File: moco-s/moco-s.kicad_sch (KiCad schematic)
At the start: 34 parts, among them J1 Conn_01x06, J2 Conn_01x02, J3 Conn_01x09, J5 Debug, SW1 SW_Push, SW2 SW_Push, U1 XC6220B331MR

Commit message: Update ref
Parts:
- renumbered C2 to C1, C6 to C2, C8 to C3, H3 to H1, H1 to H2, H4 to H3, H2 to H4, J5 to J2, J2 to J3, J3 to J4, R6 to R1, R14 to R10, R17 to R11, R18 to R12, R8 to R2, R11 to R3, R15 to R4, R16 to R5, R13 to R6, R1 to R7, R2 to R8, R3 to R9, SB7 to SB1, JP1 to SB2, JP2 to SB3, JP3 to SB4, SB4 to SB5, TP3 to TP1, TP5 to TP2

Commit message: Use kelvin connection for shunt resistance
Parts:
- C3: JLCPCB Part # (none) -> C368809; MFR.Part # (none) -> CL05A475KP5NRNC
- J1: JLCPCB Part # (none) -> C2829255; MFR.Part # (none) -> GH1.25-6PWBPZ
- J3: JLCPCB Part # (none) -> C98733; MFR.Part # (none) -> XT60
- J4: JLCPCB Part # (none) -> C2829258; MFR.Part # (none) -> GH1.25-9PWBPZ
- R7: JLCPCB Part # (none) -> C25172; MFR.Part # (none) -> 0402WGJ0561TCE
- R8, R9: JLCPCB Part # (none) -> C105876; MFR.Part # (none) -> RC0402JR-07330RL
- SB2, SB3, SB4: now left out of the parts list
- SW1, SW2: JLCPCB Part # (none) -> C520860; MFR.Part # (none) -> TS-1092S-B3D2-G
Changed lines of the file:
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@@
   (title_block
     (title "MoCo-S")
+    (rev "1.0")
   )
   (junction (at 77.47 137.16) (diameter 0) (color 0 0 0 0)
@@
   )
   (symbol (lib_id "Jumper:SolderJumper_3_Open") (at 200.66 64.77 90) (unit 1)
-    (in_bom yes) (on_board yes)
+    (in_bom no) (on_board yes)
     (property "Reference" "SB2" (id 0) (at 198.12 64.77 90)
       (effects (font (size 1.27 1.27)) (justify left))
@@
     )
     (property "Datasheet" "~" (id 3) (at 72.39 142.24 0)
+      (effects (font (size 1.27 1.27)) hide)
+    )
+    (property "JLCPCB Part #" "C520860" (id 4) (at 77.47 142.24 0)
+      (effects (font (size 1.27 1.27)) hide)
+    )
+    (property "MFR.Part #" "TS-1092S-B3D2-G" (id 5) (at 77.47 142.24 0)
       (effects (font (size 1.27 1.27)) hide)
     )
@@
     )
     (property "Datasheet" "~" (id 3) (at 41.91 133.35 0)
+      (effects (font (size 1.27 1.27)) hide)
+    )
+    (property "JLCPCB Part #" "C520860" (id 4) (at 46.99 133.35 0)
+      (effects (font (size 1.27 1.27)) hide)
+    )
+    (property "MFR.Part #" "TS-1092S-B3D2-G" (id 5) (at 46.99 133.35 0)
       (effects (font (size 1.27 1.27)) hide)
     )
@@
   )
   (symbol (lib_id "Jumper:SolderJumper_3_Open") (at 200.66 81.28 90) (unit 1)
-    (in_bom yes) (on_board yes)
+    (in_bom no) (on_board yes)
     (property "Reference" "SB3" (id 0) (at 198.12 81.28 90)
       (effects (font (size 1.27 1.27)) (justify left))
@@
     )
     (property "Note" "${REFERENCE}: Main power input" (id 4) (at 184.15 149.86 0))
+    (property "JLCPCB Part #" "C98733" (id 5) (at 185.42 143.51 0)
+      (effects (font (size 1.27 1.27)) hide)
+    )
+    (property "MFR.Part #" "XT60" (id 6) (at 185.42 143.51 0)
+      (effects (font (size 1.27 1.27)) hide)
+    )
     (pin "1")
     (pin "2")
@@
       (effects (font (size 1.27 1.27)) hide)
     )
+    (property "JLCPCB Part #" "C2829255" (id 4) (at 68.58 180.34 0)
+      (effects (font (size 1.27 1.27)) hide)
+    )
+    (property "MFR.Part #" "GH1.25-6PWBPZ" (id 5) (at 68.58 180.34 0)
+      (effects (font (size 1.27 1.27)) hide)
+    )
     (pin "1")
     (pin "2")
@@
       (effects (font (size 1.27 1.27)) hide)
     )
-    (property "JLCPCB Part #" "" (id 4) (at 243.84 148.59 0)
-      (effects (font (size 1.27 1.27)) hide)
-    )
-    (property "MFR.Part #" "" (id 5) (at 243.84 148.59 0)
+    (property "JLCPCB Part #" "C368809" (id 4) (at 243.84 148.59 0)
+      (effects (font (size 1.27 1.27)) hide)
+    )
+    (property "MFR.Part #" "CL05A475KP5NRNC" (id 5) (at 243.84 148.59 0)
       (effects (font (size 1.27 1.27)) hide)
     )
@@
   )
   (symbol (lib_id "Jumper:SolderJumper_3_Open") (at 200.66 97.79 90) (unit 1)
-    (in_bom yes) (on_board yes)
+    (in_bom no) (on_board yes)
     (property "Reference" "SB4" (id 0) (at 198.12 97.79 90)
       (effects (font (size 1.27 1.27)) (justify left))
@@
       (effects (font (size 1.27 1.27)) hide)
     )
+    (property "JLCPCB Part #" "C105876" (id 4) (at 119.38 147.32 0)
+      (effects (font (size 1.27 1.27)) hide)
+    )
+    (property "MFR.Part #" "RC0402JR-07330RL" (id 5) (at 119.38 147.32 0)
+      (effects (font (size 1.27 1.27)) hide)
+    )
     (pin "1")
     (pin "2")
@@
       (effects (font (size 1.27 1.27)) hide)
     )
+    (property "JLCPCB Part #" "C25172" (id 4) (at 119.38 142.24 0)
+      (effects (font (size 1.27 1.27)) hide)
+    )
+    (property "MFR.Part #" "0402WGJ0561TCE" (id 5) (at 119.38 142.24 0)
+      (effects (font (size 1.27 1.27)) hide)
+    )
     (pin "1")
     (pin "2")
@@
     )
     (property "Datasheet" "~" (id 3) (at 265.43 82.55 0)
+      (effects (font (size 1.27 1.27)) hide)
+    )
+    (property "JLCPCB Part #" "C2829258" (id 4) (at 265.43 82.55 0)
+      (effects (font (size 1.27 1.27)) hide)
+    )
+    (property "MFR.Part #" "GH1.25-9PWBPZ" (id 5) (at 265.43 82.55 0)
       (effects (font (size 1.27 1.27)) hide)
     )
@@
       (effects (font (size 1.27 1.27)) hide)
     )
+    (property "JLCPCB Part #" "C105876" (id 4) (at 119.38 144.78 0)
+      (effects (font (size 1.27 1.27)) hide)
+    )
+    (property "MFR.Part #" "RC0402JR-07330RL" (id 5) (at 119.38 144.78 0)
+      (effects (font (size 1.27 1.27)) hide)
+    )
     (pin "1")
     (pin "2")
@@
     )
     (path "/5f858a64-8e5c-4641-b09d-942a81494abe/862e470f-2a50-4080-868f-57a760d2109b"
-      (reference "C43") (unit 1) (value "1uF/25V") (footprint "Capacitor_SMD:C_0402_1005Metric")
+      (reference "C43") (unit 1) (value "1uF") (footprint "Capacitor_SMD:C_0402_1005Metric")
     )
     (path "/f7ad0ebf-8e81-44cc-8ff1-e4ac32df718d/15958ae8-4247-4024-8bde-df63d8dfca95"

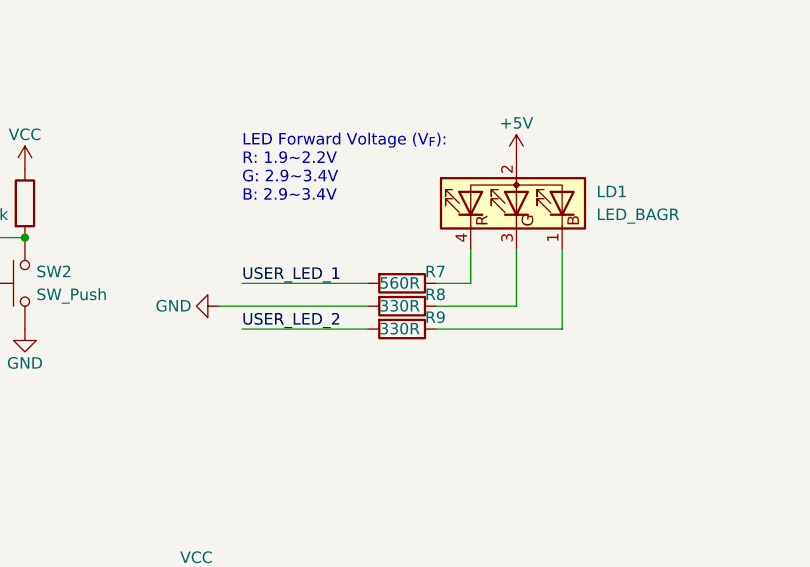
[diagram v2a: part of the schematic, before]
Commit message: Replace some extended parts to basic parts
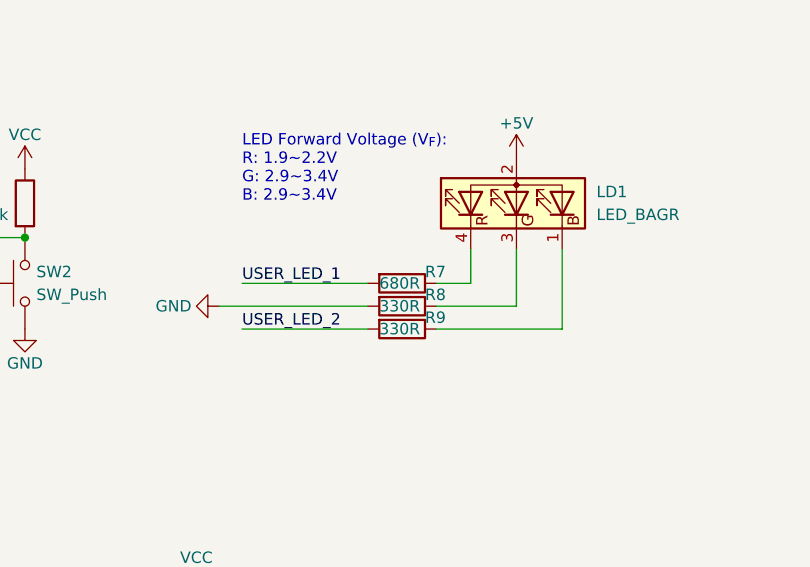
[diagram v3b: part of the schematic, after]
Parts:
- C1, J3, J4, LD1, SW1, SW2, U1: Basic Part (none) -> N
- C2, H1, H2, H3, H4, J1, J2, R1, R10, R11, R12, R2, R3, R4, R5, R6, SB2, SB3, SB4: Basic Part (none) -> Y
- C3: Basic Part (none) -> Y; JLCPCB Part # C368809 -> C23733; MFR.Part # CL05A475KP5NRNC -> CL05A475MP5NRNC
- R7: value 560R -> 680R; Basic Part (none) -> Y; JLCPCB Part # C25172 -> C25130; MFR.Part # 0402WGJ0561TCE -> 0402WGF6800TCE
- R8, R9: Basic Part (none) -> Y; JLCPCB Part # C105876 -> C25104; MFR.Part # RC0402JR-07330RL -> 0402WGF3300TCE
